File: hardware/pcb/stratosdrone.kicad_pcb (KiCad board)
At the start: 4 copper layers, 36 x 70 mm, 115 parts, among them J1 BATT_PH2, J10 DBG, J11 C6DBG, J2 USB-C-16P, J3 FLOW_HDR, J4 CAM_FFC15, J5 MOTOR1, J6 MOTOR2, J7 MOTOR3, J8 MOTOR4, J9 EXP, Q1 AO3400A, Q2 AO3400A, Q3 AO3400A, Q4 AO3400A, SW1 RESET, SW2 BOOT, U1 ESP32-P4NRW32, U10 TLV62569DBVR, U2 W25Q128JVSIQ, U3 ESP32-C6-MINI-1, U4 TP4056-42-ESOP8, U5 SY8089AAAC, U6 ICM-42688-P, U7 SPL06-001, U8 VL53L1X, U9 PMW3901MB, Y1 40MHz

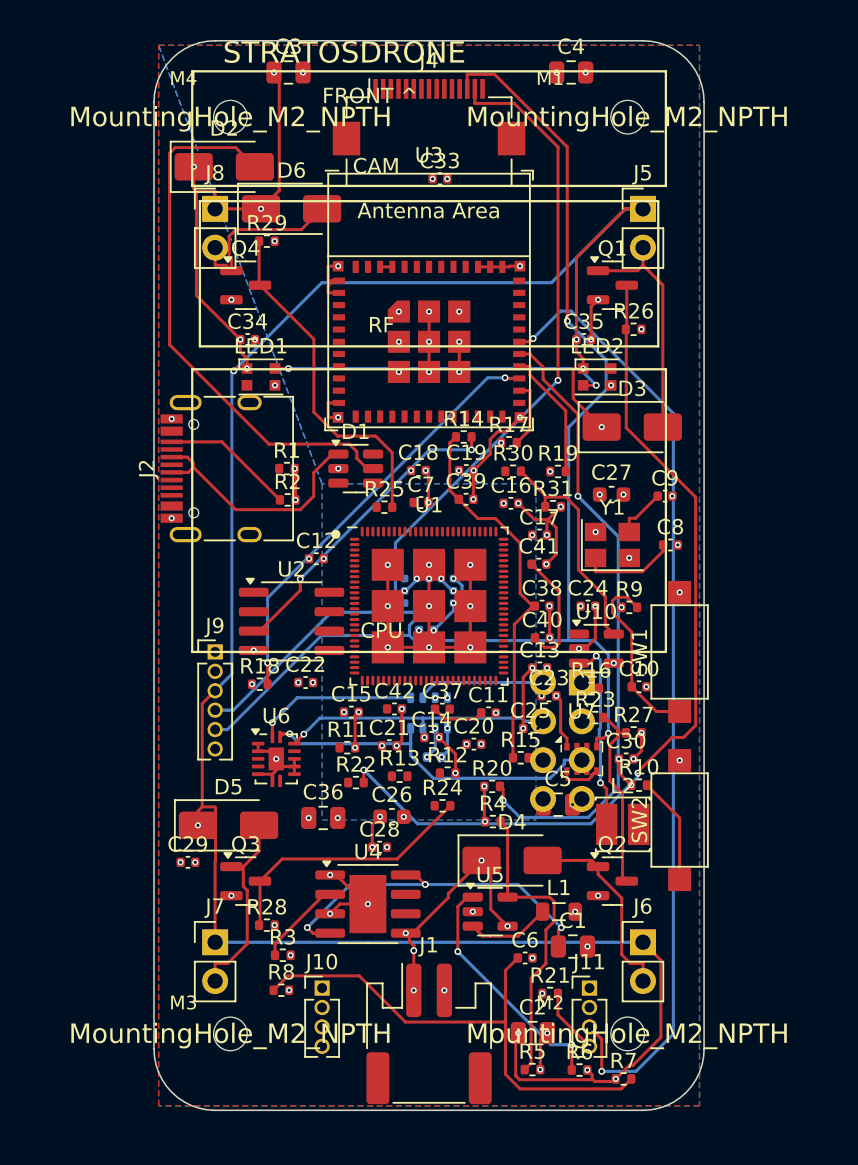
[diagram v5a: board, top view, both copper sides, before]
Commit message: hardware/pcb: courtyard-aware placement — zero body overlaps
Follow-up to the boundary fix: the user still saw parts that looked cramped.
Cause: the placer only avoided PAD overlaps (pad extent + 0.25 mm), so module
bodies/keepouts and tall connector courtyards still touched.

Engine now places on real COURTYARDS:
- Collision size = the footprint's own courtyard graphics (body + IPC clearance
  + module keepouts like the ESP32-C6 antenna), pad+0.5 mm fallback.
- place() swaps the collision box for 90/270 anchors (USB-C, switches) — these
  rotated parts were sized wrong before.
- cur_box() in the repair pass reads courtyard graphics directly (GetCourtyard()
  has no in-memory cache pre-save, so it was silently using pad boxes).
- find_slot() now rings out to the full board and its grid fallback is
  distance-sorted, so a part that can't sit by its anchor lands at the nearest
  free spot instead of being dumped in a corner.

Placement tweaks: U3 (ESP32-C6) spaced down so its antenna keepout clears the
camera FFC; LED1 to a clear top-left spot; motor FETs shifted 2 mm off their
edge headers. D2 (DNP wide D_SMA) had no 7 mm gap left anywhere on top, so it
moves to the empty bottom-left, clear of the downward sensor windows.

Result: all 111 pads inside the outline, zero same-side pad overlaps, **zero
courtyard overlaps >0.3 mm**, tightest body gap 0.35 mm. assert_placement now
reports "no significant courtyard overlaps".

Routing is regenerated on this placement in a follow-up commit; dsn re-exported.

Co-Authored-By: Claude Opus 4.8 <noreply@anthropic.com>
Claude-Session: https://claude.ai/code/session_011szEEHZ8KTTsZmGFgY6Cjw
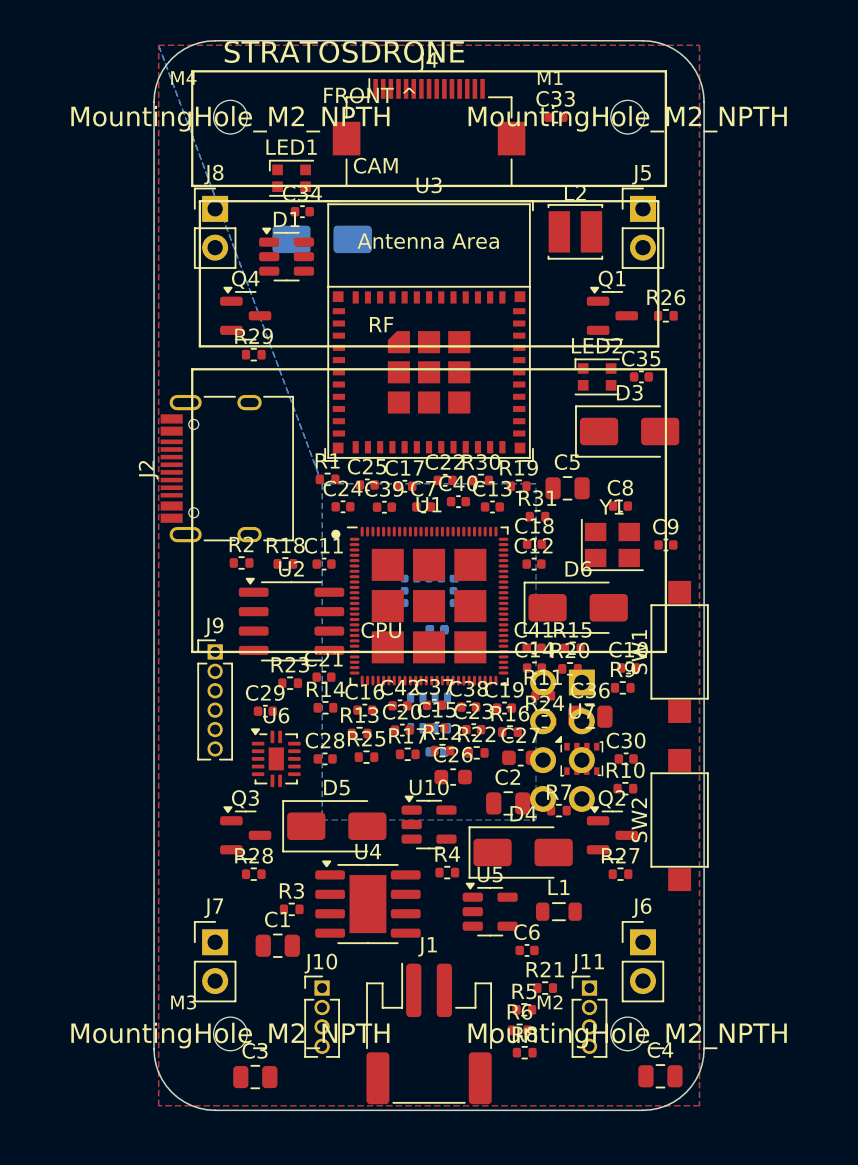
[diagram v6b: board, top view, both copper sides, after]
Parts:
- D2: moved to B.Cu
- moved C4 66.0 mm to (33.1, 67.8)
- moved C3 65.8 mm to (6.63, 67.8)
- moved L2 38.9 mm to (27.6, 12.5)
- moved D6 32.1 mm to (27.8, 37.1)
- moved R17 21.4 mm to (16.6, 46.7)
- moved C5 20.7 mm to (27.1, 29.3)
- moved R23 20.1 mm to (8.91, 42.0)
- moved R14 19.9 mm to (11.2, 43.7)
- moved C1 19.3 mm to (8.10, 59.2)
- moved C25 19.2 mm to (14.0, 29.1)
- moved C36 18.7 mm to (28.6, 44.2)
- moved C27 18.2 mm to (24.0, 46.9)
- moved R7 18.1 mm to (26.5, 50.4)
- moved C24 17.3 mm to (12.4, 30.5)
- moved C16 16.6 mm to (13.8, 43.8)
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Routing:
- net VBAT: track 186.1 -> 0.00 mm, vias 23 -> 0
- net GND: track 99.5 -> 0.00 mm, vias 112 -> 0
- net I2C_SCL: track 82.7 -> 0.00 mm, vias 2 -> 0
- net C6_U0RXD: track 63.2 -> 0.00 mm, vias 2 -> 0
- net I2C_SDA: track 59.4 -> 0.00 mm, vias 1 -> 0
- net VBUS: track 59.2 -> 0.00 mm, vias 3 -> 0
- net M1_GATE: track 57.6 -> 0.00 mm, vias 2 -> 0
- net SDIO_D3: track 41.3 -> 0.00 mm, vias 2 -> 0
- net VBAT_SENSE: track 33.7 -> 0.00 mm
- net SDIO_D1: track 28.1 -> 0.00 mm, vias 2 -> 0
- net VDD_FLASHIO: track 24.8 -> 0.00 mm
- net SPI_MOSI: track 23.2 -> 0.00 mm, vias 1 -> 0
- net M4_GATE: track 22.5 -> 0.00 mm
- net LED_D12: track 22.3 -> 0.00 mm, vias 2 -> 0
- net 3V3: track 20.6 -> 0.00 mm, vias 43 -> 0
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
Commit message: hardware/pcb: re-route on the clean (courtyard-aware) placement
Freerouting 1.9 on the re-exported DSN: 231 wires / 22 vias -> 530 track
segments + 22 vias imported; connect_power() adds 176 stitch vias; zones
filled; 14 gerbers + drill re-exported. After fill+stitch: 104 ratsnest
connections remain (221 pre-fill) — same partial-autoroute status as before,
now on a placement with zero pad/courtyard overlaps. KNOWN_GAPS items 1 and 2
updated.

Co-Authored-By: Claude Opus 4.8 <noreply@anthropic.com>
Claude-Session: https://claude.ai/code/session_011szEEHZ8KTTsZmGFgY6Cjw
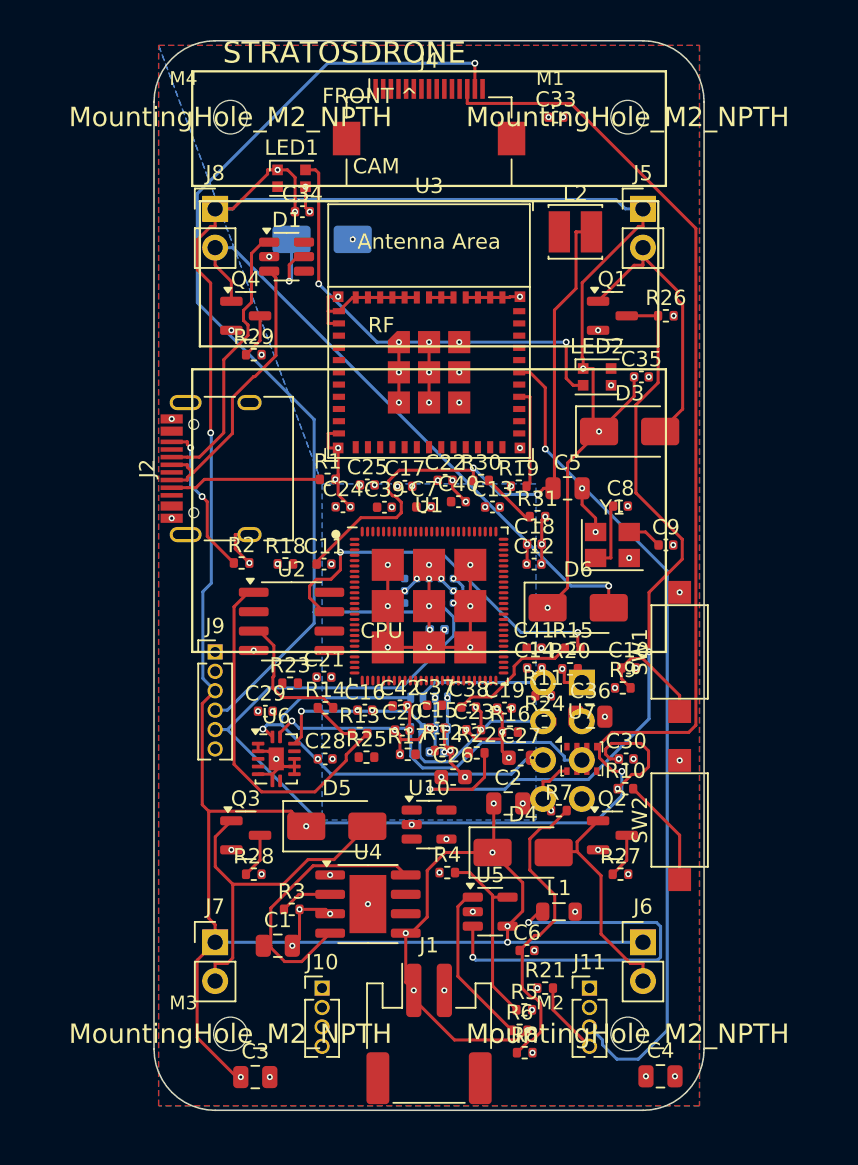
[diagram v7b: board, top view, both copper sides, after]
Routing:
- net VBAT: track 0.00 -> 201.2 mm, vias 0 -> 23
- net I2C_SCL: track 0.00 -> 112.8 mm, vias 0 -> 1
- net GND: track 0.00 -> 89.8 mm, vias 0 -> 112
- net I2C_SDA: track 0.00 -> 71.4 mm, vias 0 -> 1
- net C6_U0RXD: track 0.00 -> 54.4 mm, vias 0 -> 1
- net M1_GATE: track 0.00 -> 52.9 mm, vias 0 -> 2
- net VDD_CORE: track 0.00 -> 40.7 mm, vias 0 -> 2
- net M4_D: track 0.00 -> 40.3 mm, vias 0 -> 1
- net 3V3: track 0.00 -> 30.6 mm, vias 0 -> 43
- net SPI_MISO: track 0.00 -> 30.5 mm, vias 0 -> 1
- net LED_D12: track 0.00 -> 29.6 mm, vias 0 -> 2
- net SW3V3: track 0.00 -> 26.4 mm, vias 0 -> 2
- net FLASH_IO3: track 0.00 -> 24.9 mm, vias 0 -> 2
- net SPI_MOSI: track 0.00 -> 24.0 mm, vias 0 -> 1
- net VBUS: track 0.00 -> 23.4 mm, vias 0 -> 1
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
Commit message: Improve power stitch via clearance checking and export gerbers
- Rewrite connect_power() to be layer-aware: only stitch pads whose net lacks a copper pour on the pad's own layer (GND on F.Cu already has pour, so skip those; 3V3/VBAT get vias)
- Add accurate rectangle+segment distance checks: each via candidate is dropped if any different-net pad/track/via sits within 0.25mm (clearance margin)
- Reduce vias from 176 (33 DRC violations) to 43 (0 violations) while preserving cross-layer power connectivity
- Re-export gerbers with filled zones: 14 files ready for JLCPCB

Board state:
- 530 routed track segments (Freerouting 1.9)
- 43 power stitch vias (0 DRC violations)
- 137 unconnected ratsnest (expected for dense 2-signal-layer prototype; user to finish in KiCad)

Co-Authored-By: Claude Fable 5 <noreply@anthropic.com>
Claude-Session: https://claude.ai/code/session_011szEEHZ8KTTsZmGFgY6Cjw
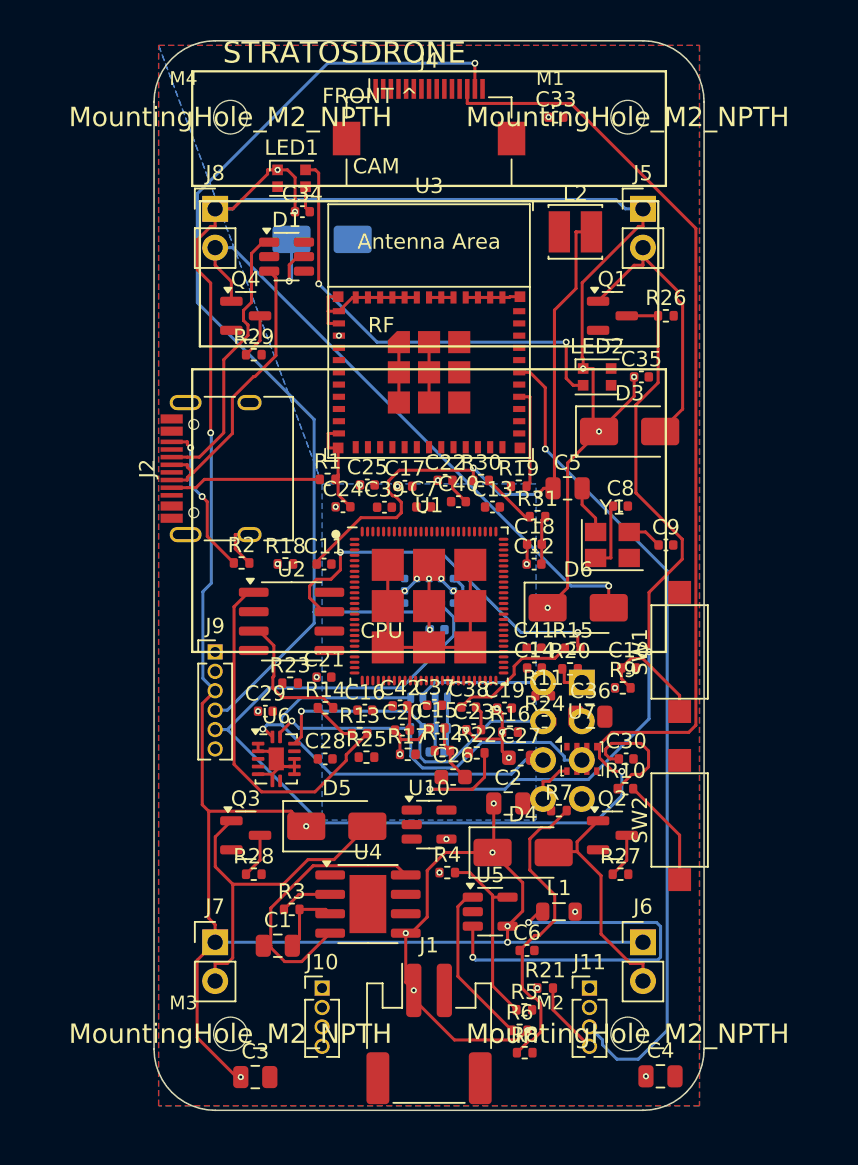
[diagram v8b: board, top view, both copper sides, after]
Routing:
- net VBAT: vias 23 -> 16
- net GND: vias 112 -> 6
- net 3V3: vias 43 -> 21
